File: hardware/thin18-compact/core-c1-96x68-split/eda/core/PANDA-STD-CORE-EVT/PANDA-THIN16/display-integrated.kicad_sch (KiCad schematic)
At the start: 57 parts, among them J601 DF40C-60DS-0.4V(58), J802 FH12-24S-0.5SH(55), J804 FH34SRJ-6S-0.5SH(50), Q801 NX3008NBK,215, U801 AIP74LVC2G17GC363.TR, U802 AIP74LVC2G17GC363.TR, U803 AIP74LVC2G17GC363.TR, U905 SGM37601YTRL20G/TR

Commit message: feat(hw): audit split stack and verify exact-part sourcing
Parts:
- J601: LCSC (none) -> C2880473

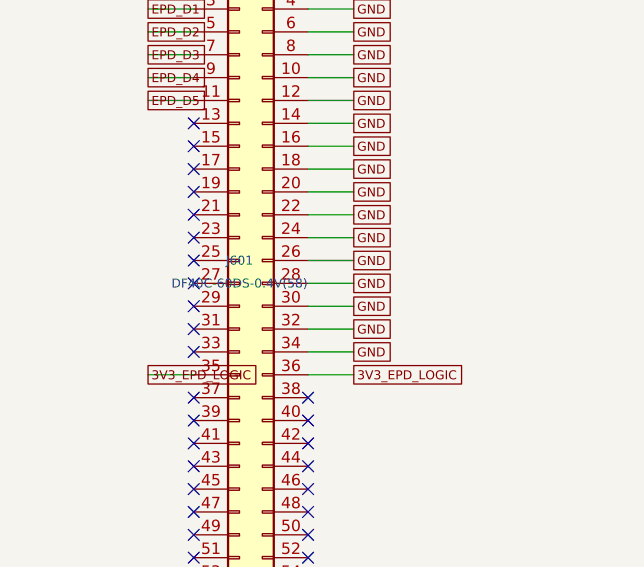
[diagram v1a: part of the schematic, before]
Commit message: hw: apply reviewed domestic ECOs and gate incomplete Split-C1 orders
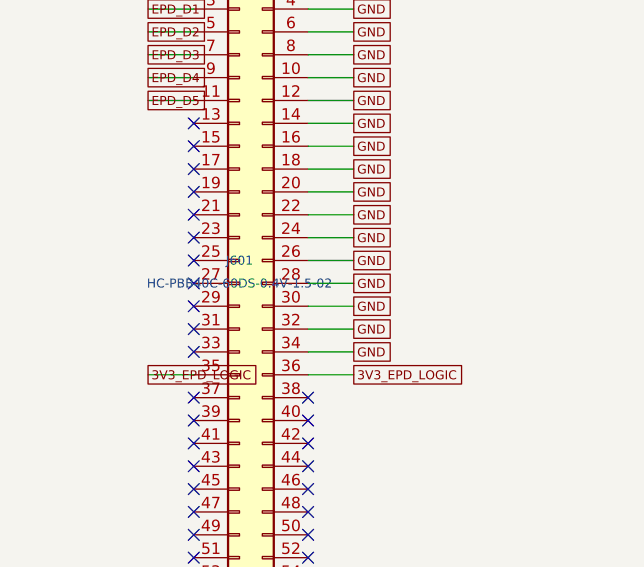
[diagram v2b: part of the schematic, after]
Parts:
- J601: value DF40C-60DS-0.4V(58) -> HC-PBB40C-60DS-0.4V-1.5-02; footprint Connector_Hirose_DF40:Hirose_DF40C-60DS-0.4V_2x30_P0.4mm -> panda-standard:HCTL_PBB40C_60DS_04V_15; LCSC C2880473 -> C19089250; MPN DF40C-60DS-0.4V(58) -> HC-PBB40C-60DS-0.4V-1.5-02; Manufacturer Hirose -> HCTL

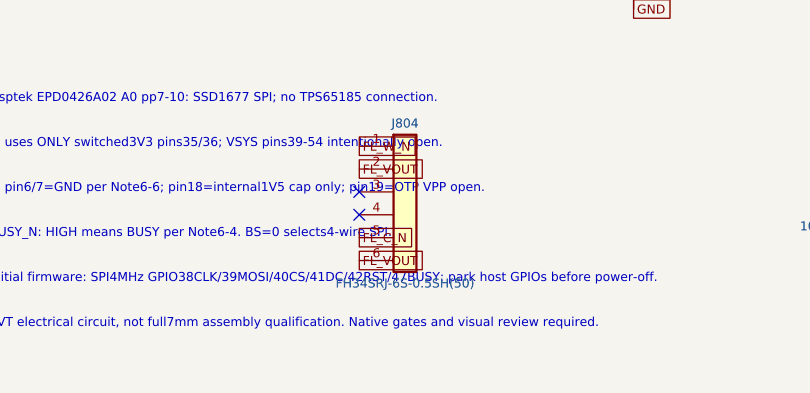
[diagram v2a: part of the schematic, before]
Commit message: hw: apply domestic wire, FPC and inductor ECOs with replay guards
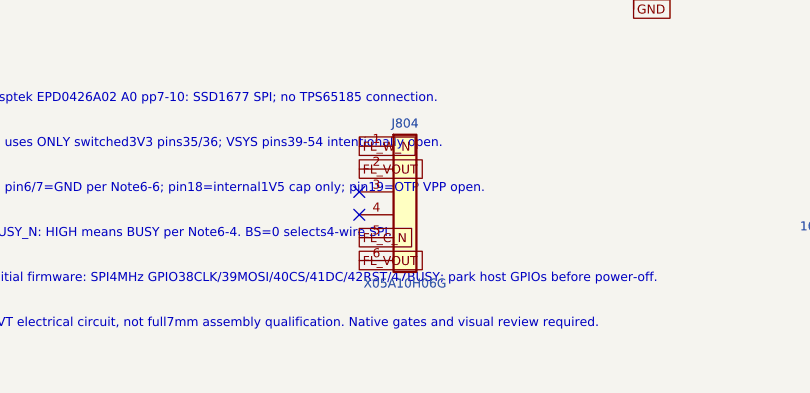
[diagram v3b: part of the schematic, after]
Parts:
- J804: value FH34SRJ-6S-0.5SH(50) -> X05A10H06G; footprint PandaDomestic:FH34SRJ-6S-0.5SH_50 -> panda-standard:XKB_X05A10H06G_A2; LCSC C224194 -> C528032; MPN FH34SRJ-6S-0.5SH(50) -> X05A10H06G; Manufacturer Hirose -> XKB Connection; Qualification Exact C224194 land pattern; FT01C FPC orientation and inser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 -> Manufacturer X05A10HXX p2 A2, ECN-P-2026011502 dated2026-01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
